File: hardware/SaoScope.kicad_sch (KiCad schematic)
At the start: 24 parts, among them J1 Conn_01x03_Pin, J2 Conn_01x04_Socket, SW1 TS-1077S-AR02016, SW2 TS-1077S-AR02016, SW3 TS-1077S-AR02016, SW4 TS-1077S-AR02016, SW5 TS-1077S-AR02016, U1 STM32G030F6Px, U2 LMC7660, U3 OPA197xDBV, U4 AP2120N-3.0TRG1, X1 Simple_Addon_v2

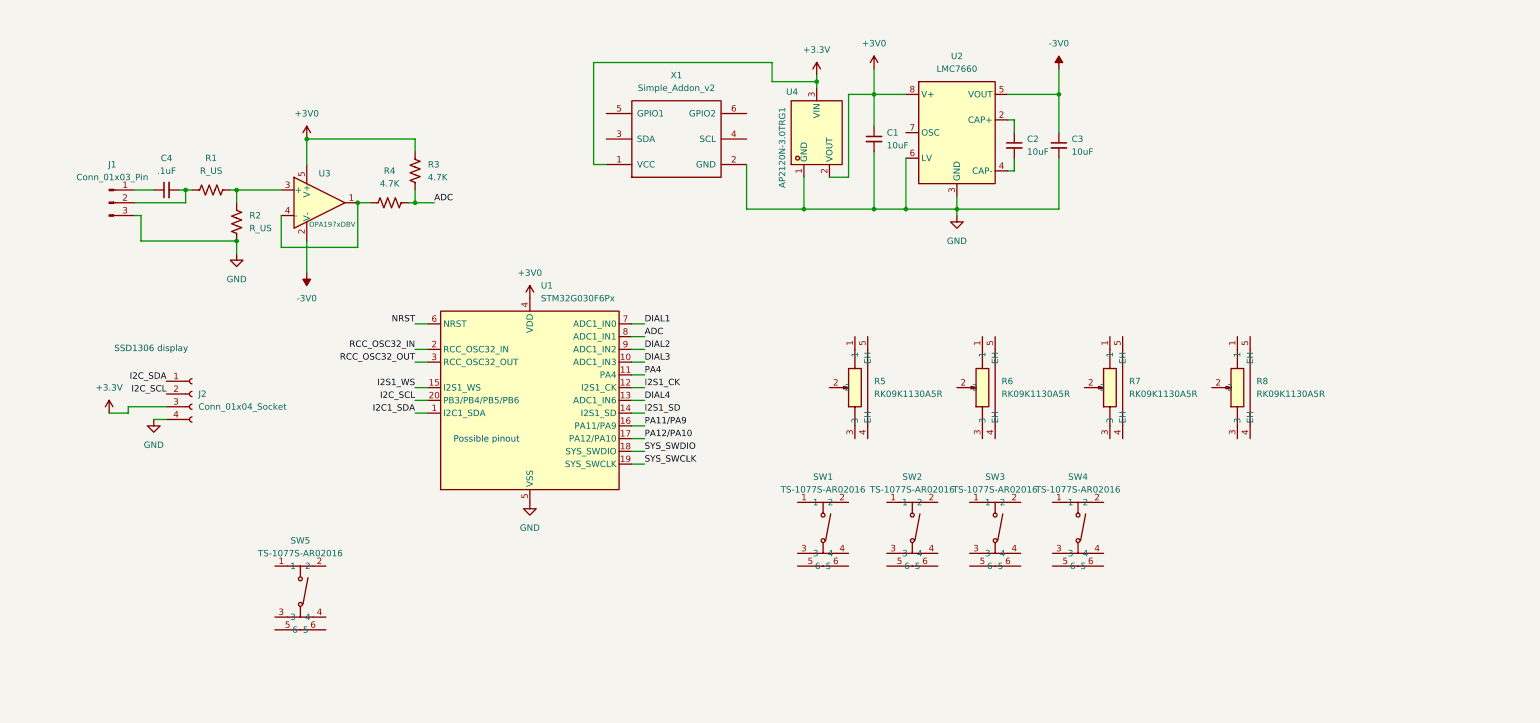
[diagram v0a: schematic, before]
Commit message: wire up pots and buttons, comments
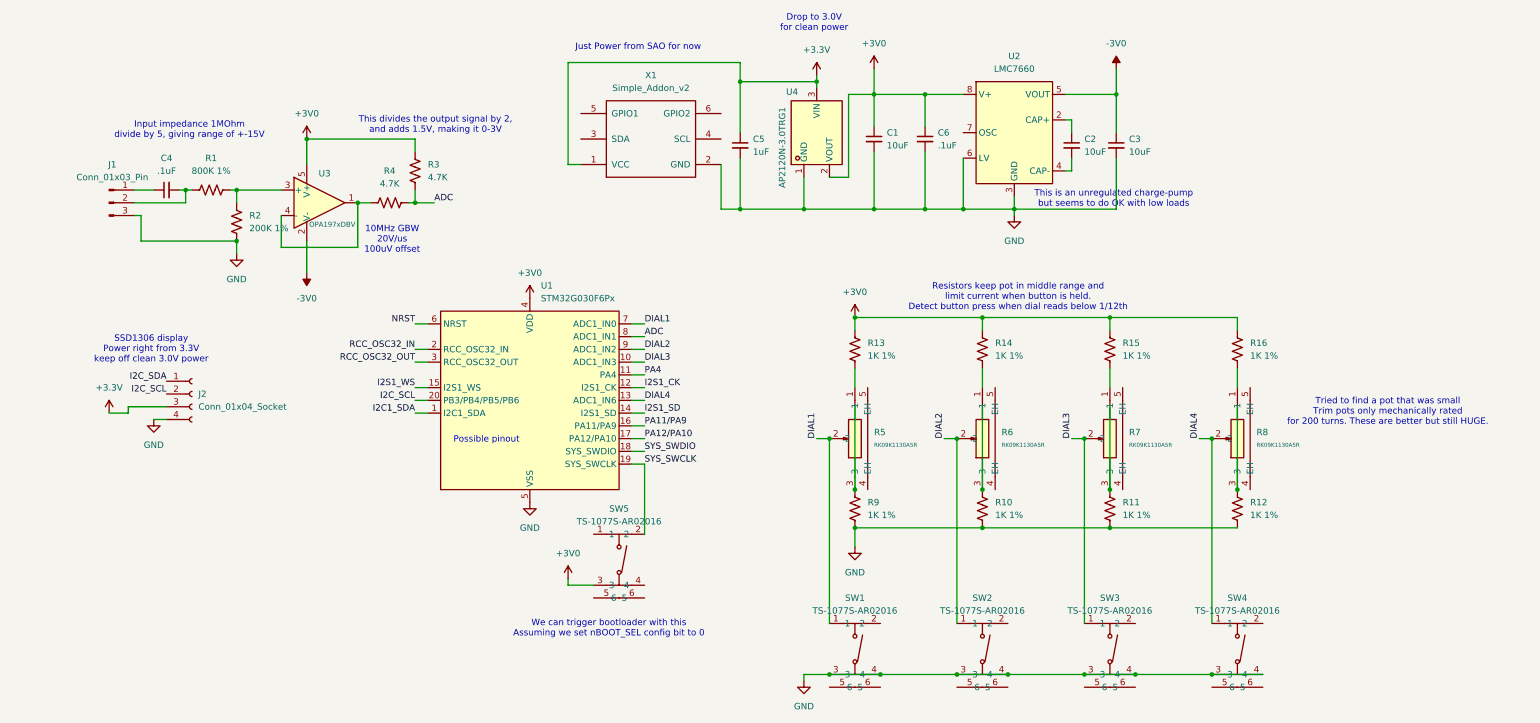
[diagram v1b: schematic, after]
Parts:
- added C5: 1uF, Capacitor_SMD:C_0603_1608Metric, symbol Device:C_Small
- added C6: .1uF, Capacitor_SMD:C_0402_1005Metric, symbol Device:C_Small
- added R10, R11, R12, R13, R14, R15, R16, R9: 1K 1%, Resistor_SMD:R_0402_1005Metric, symbol Device:R_US
- C1, C2, C3: footprint (none) -> Capacitor_SMD:C_0805_2012Metric
- C4: footprint (none) -> Capacitor_SMD:C_0402_1005Metric
- R1: value R_US -> 800K 1%; footprint (none) -> Resistor_SMD:R_0402_1005Metric
- R2: value R_US -> 200K 1%; footprint (none) -> Resistor_SMD:R_0402_1005Metric
- R3, R4: footprint (none) -> Resistor_SMD:R_0402_1005Metric
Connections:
- net +3.3V: now also C5.1
- net +3V0: now also SW5.3, C6.1, R13.1, R14.1, R15.1, R16.1
- net DIAL1: now also R5.2, SW1.1
- net DIAL2: now also R6.2, SW2.1
- net DIAL3: now also R7.2, SW3.1
- net DIAL4: now also R8.2, SW4.1
- net GND: now also SW1.3, SW1.4, SW2.3, SW2.4, SW3.3, SW3.4, SW4.3, SW4.4, C5.2, C6.2, R10.2, R11.2, R12.2, R9.2
- net SYS_SWCLK: now also SW5.2
- net at R5.1: now also R13.2
- net at R5.3: now also R9.1
- net at R6.1: now also R14.2
- net at R6.3: now also R10.1
- net at R7.1: now also R15.2
- net at R7.3: now also R11.1
- net at R8.1: now also R16.2
- net at R8.3: now also R12.1
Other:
- note added: "10MHz GBW 20V/us 100uV offset"
- note added: "Drop to 3.0V for clean power"
- note added: "Input impedance 1MOhm divide by 5, giving range of +-15V"
- note added: "Just Power from SAO for now"
- note added: "Resistors keep pot in middle range and limit current when button is held. Detect button press when dial reads below 1/12th"
- note added: "SSD1306 display Power right from 3.3V keep off clean 3.0V power"
- note added: "This divides the output signal by 2, and adds 1.5V, making it 0-3V"
- note added: "This is an unregulated charge-pump but seems to do OK with low loads"
- note added: "Tried to find a pot that was small Trim pots only mechanically rated for 200 turns. These are better but still HUGE."
- note added: "We can trigger bootloader with this Assuming we set nBOOT_SEL config bit to 0"
- note removed: "SSD1306 display"
- moved on the sheet: C2, C3, R5, R6, R7, R8, SW1, SW2, SW3, SW4, SW5, U2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

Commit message: basic rev
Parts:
- removed R10, R11, R12, R13, R14, R15, R16, R9: 1K 1%, Resistor_SMD:R_0402_1005Metric, symbol Device:R_US
- added C7: .1uF, Capacitor_SMD:C_0402_1005Metric, symbol Device:C_Small
- added C8, C9: 15pf, Capacitor_SMD:C_0402_1005Metric, symbol Device:C_Small
- added RN1, RN2: 1K, Resistor_SMD:R_Array_Convex_4x0402, symbol Device:R_Pack04_Split
- added TP1, TP2, TP3, TP4, TP5: TestPoint, TestPoint:TestPoint_Pad_1.5x1.5mm, symbol Connector:TestPoint
- added Y1: Crystal, Crystal:Crystal_SMD_3215-2Pin_3.2x1.5mm, symbol Device:Crystal
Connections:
- net I2C_SDA is gone; now on net I2C1_SDA: J2.1 (Pin_1)
- net +3.3V: now also TP1.1
- net +3V0: now also SW5.4, C7.1, RN1.6 (R3.2), RN1.8 (R1.2), RN2.6 (R3.2), RN2.8 (R1.2)
- net -3V0: now also C7.2
- net DIAL1: now also SW1.2
- net DIAL2: now also SW2.2
- net DIAL3: now also SW3.2
- net DIAL4: now also SW4.2
- net GND: now also C8.1, C9.1, RN1.5 (R4.2), RN1.7 (R2.2), RN2.5 (R4.2), RN2.7 (R2.2), TP2.1
- net NRST: now also TP5.1
- net SYS_SWCLK: now also SW5.1, TP4.1
- net SYS_SWDIO: now also TP3.1
- net at R6.1: now also RN1.3 (R3.1)
- net at R7.3: now also RN2.2 (R2.1)
- net at J1.2 (Pin_2), R1.1: now also C4.1; no longer C4.2
- net at R8.1: now also RN2.3 (R3.1)
- net at R8.3: now also RN2.4 (R4.1)
- net at J1.1 (Pin_1): now also C4.2; no longer C4.1
- net at R5.3: now also RN1.2 (R2.1)
- net at R7.1: now also RN2.1 (R1.1)
- net at R5.1: now also RN1.1 (R1.1)
- net at R6.3: now also RN1.4 (R4.1)
- net I2C_SCL renamed I2C1_SCL
- net RCC_OSC32_IN: no longer names the net of U1.2 (PC14/PB9)
- net RCC_OSC32_IN: now also C8.2, Y1.1
- net RCC_OSC32_OUT: no longer names the net of U1.3 (PC15)
- net RCC_OSC32_OUT: now also C9.2, Y1.2
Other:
- moved on the sheet: C4

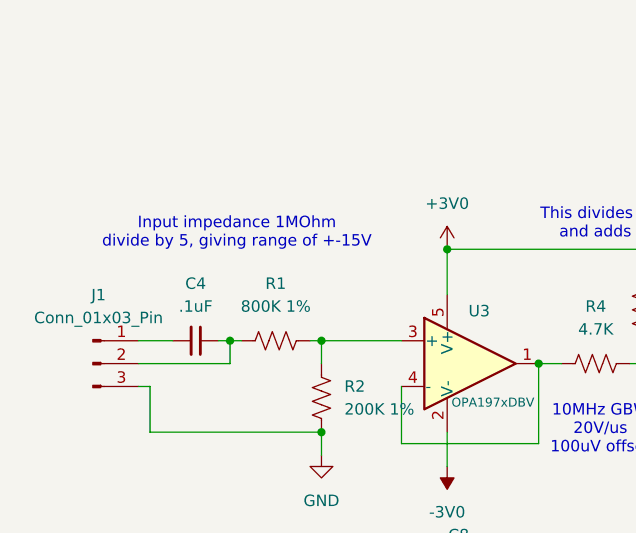
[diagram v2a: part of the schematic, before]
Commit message: switch 800k with two 1.6M resistors
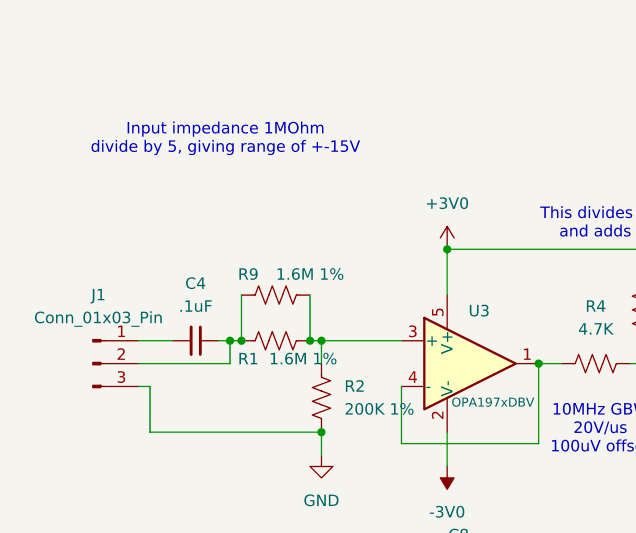
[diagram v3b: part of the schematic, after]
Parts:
- added R9: 1.6M 1%, Resistor_SMD:R_0402_1005Metric, symbol Device:R_US
- R1: value 800K 1% -> 1.6M 1%; LCSC Part (none) -> C172161
- R2: LCSC Part (none) -> C25764
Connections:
- net at C4.1, J1.2 (Pin_2), R1.1: now also R9.1
- net at R1.2, R2.1, U3.3 (+): now also R9.2
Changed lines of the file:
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@@
 	)
 	(junction
+		(at 53.34 63.5)
+		(diameter 0)
+		(color 0 0 0 0)
+	)
+	(junction
 		(at 62.23 73.66)
 		(diameter 0)
@@
 	)
 	(junction
+		(at 60.96 63.5)
+		(diameter 0)
+		(color 0 0 0 0)
+	)
+	(junction
 		(at 162.56 41.91)
 		(diameter 0)
@@
 	(wire
 		(pts
+			(xy 60.96 58.42) (xy 60.96 63.5)
+		)
+		(stroke
+			(width 0)
+			(type default)
+		)
+	)
+	(wire
+		(pts
 			(xy 76.2 73.66) (xy 76.2 77.47)
 		)
@@
 	(wire
 		(pts
+			(xy 53.34 58.42) (xy 53.34 63.5)
+		)
+		(stroke
+			(width 0)
+			(type default)
+		)
+	)
+	(wire
+		(pts
 			(xy 143.51 97.79) (xy 140.97 97.79)
 		)
@@
 	(text "Input impedance 1MOhm\ndivide by 5, giving range of +-15V"
 		(exclude_from_sim no)
-		(at 52.832 51.562 0)
+		(at 51.562 41.148 0)
 		(effects
 			(font
@@
 	)
 	(symbol
+		(lib_id "Device:R_US")
+		(at 57.15 58.42 90)
+		(unit 1)
+		(exclude_from_sim no)
+		(in_bom yes)
+		(on_board yes)
+		(dnp no)
+		(property "Reference" "R9"
+			(at 54.102 56.134 90)
+			(effects
+				(font
+					(size 1.27 1.27)
+				)
+			)
+		)
+		(property "Value" "1.6M 1%"
+			(at 60.96 56.134 90)
+			(effects
+				(font
+					(size 1.27 1.27)
+				)
+			)
+		)
+		(property "Footprint" "Resistor_SMD:R_0402_1005Metric"
+			(at 57.404 57.404 90)
+			(effects
+				(font
+					(size 1.27 1.27)
+				)
+				(hide yes)
+			)
+		)
+		(property "Datasheet" "~"
+			(at 57.15 58.42 0)
+			(effects
+				(font
+					(size 1.27 1.27)
+				)
+				(hide yes)
+			)
+		)
+		(property "Description" "Resistor, US symbol"
+			(at 57.15 58.42 0)
+			(effects
+				(font
+					(size 1.27 1.27)
+				)
+				(hide yes)
+			)
+		)
+		(property "LCSC Part" "C172161"
+			(at 57.15 58.42 90)
+			(effects
+				(font
+					(size 1.27 1.27)
+				)
+				(hide yes)
+			)
+		)
+		(pin "1"
+		)
+		(pin "2"
+		)
+		(instances
+			(project "SaoScope"
+				(path "/a633a3cb-d3b7-422b-9438-b60cd33ff473"
+					(reference "R9")
+					(unit 1)
+				)
+			)
+		)
+	)
+	(symbol
 		(lib_id "Device:R_Pack04_Split")
 		(at 261.62 127 180)
@@
 		(on_board yes)
 		(dnp no)
-		(fields_autoplaced yes)
 		(property "Reference" "R1"
-			(at 57.15 57.15 90)
+			(at 54.102 65.532 90)
 			(effects
 				(font
@@
 			)
 		)
-		(property "Value" "800K 1%"
-			(at 57.15 59.69 90)
+		(property "Value" "1.6M 1%"
+			(at 60.198 65.532 90)
 			(effects
 				(font
@@
 			)
 		)
+		(property "LCSC Part" "C172161"
+			(at 57.15 63.5 90)
+			(effects
+				(font
+					(size 1.27 1.27)
+				)
+				(hide yes)
+			)
+		)
 		(pin "1"
 		)
@@
 			(at 62.23 69.85 0)
 			(effects
+				(font
+					(size 1.27 1.27)
+				)
+				(hide yes)
+			)
+		)
+		(property "LCSC Part" "C25764"
+			(at 62.23 69.85 0)
+			(effects

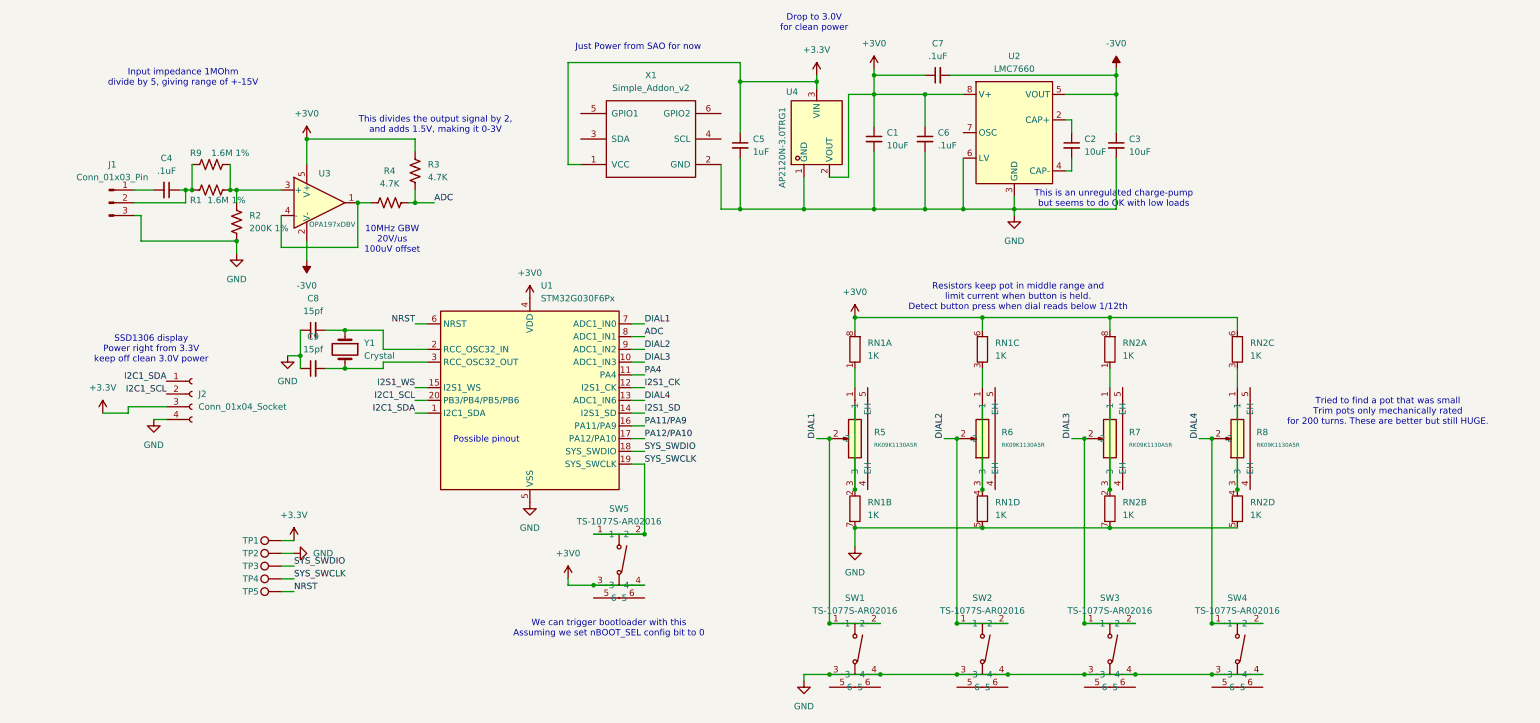
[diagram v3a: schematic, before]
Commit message: bring in i2c lines from sao, a gpio, and run a sig gen line out. rework button labels.
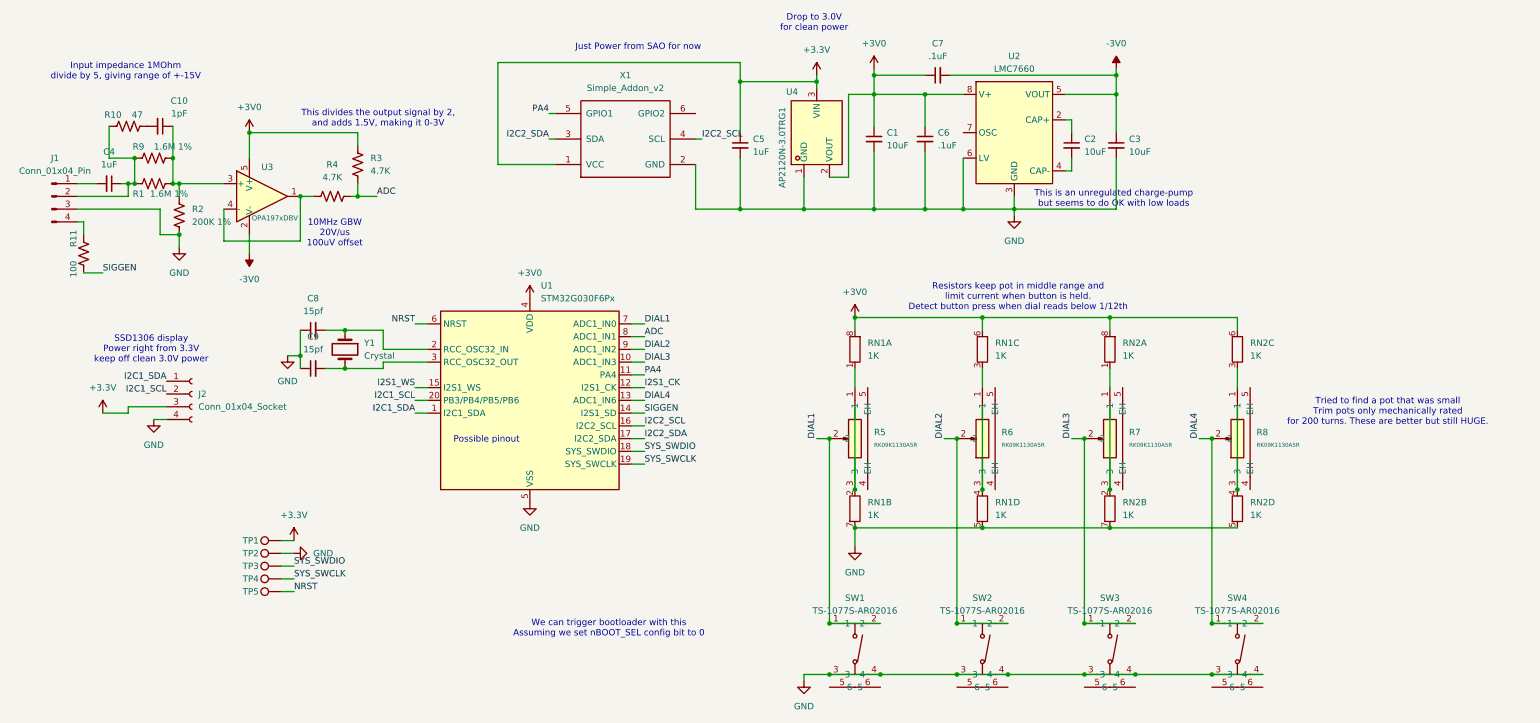
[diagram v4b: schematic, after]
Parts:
- removed J1: Conn_01x03_Pin, Connector_PinHeader_2.54mm:PinHeader_1x03_P2.54mm_Vertical, symbol Connector:Conn_01x03_Pin
- removed SW5: TS-1077S-AR02016, easyeda2kicad:KEY-SMD_4P-L3.1-W3.1-P2.00-LS4.0, symbol easyeda2kicad:TS-1077S-AR02016
- added C10: 1pF, Capacitor_SMD:C_0402_1005Metric, symbol Device:C_Small
- added J1: Conn_01x04_Pin, Connector_PinHeader_2.54mm:PinHeader_1x04_P2.54mm_Vertical, symbol Connector:Conn_01x04_Pin
- added R10: 47, Resistor_SMD:R_0402_1005Metric, symbol Device:R_US
- added R11: 100, Resistor_SMD:R_0402_1005Metric, symbol Device:R_US
- C4: value .1uF -> 1uF; footprint Capacitor_SMD:C_0402_1005Metric -> Capacitor_SMD:C_0603_1608Metric
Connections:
- net PA11/PA9 is gone; now on net I2C2_SCL: U1.16 (PA11/PA9)
- net PA12/PA10 is gone; now on net I2C2_SDA: U1.17 (PA12/PA10)
- net GND: now also J1.3 (Pin_3)
- net PA4: now also X1.5 (GPIO1)
- net at C4.1, R1.1, R9.1: now also J1.2 (Pin_2), R10.1
- net at R1.2, R2.1, R9.2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: now also C10.1
- net at C4.2: now also J1.1 (Pin_1)
- net I2C2_SDA: now reaches X1.3 (SDA)
- net I2C2_SCL: now reaches X1.4 (SCL)
- net I2S1_SD renamed SIGGEN
- net SIGGEN: now also R11.2
- new net: C10.2, R10.2
- new net: J1.4 (Pin_4), R11.1
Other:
- moved on the sheet: C4, R1, R2, R3, R4, R9, U3, X1

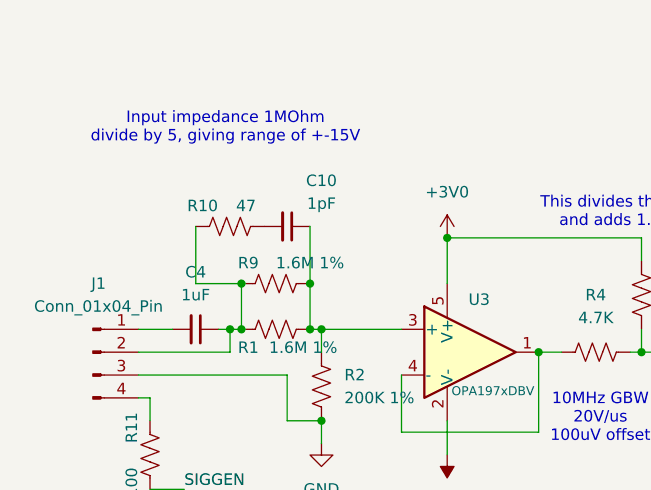
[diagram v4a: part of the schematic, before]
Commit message: fix part number oops
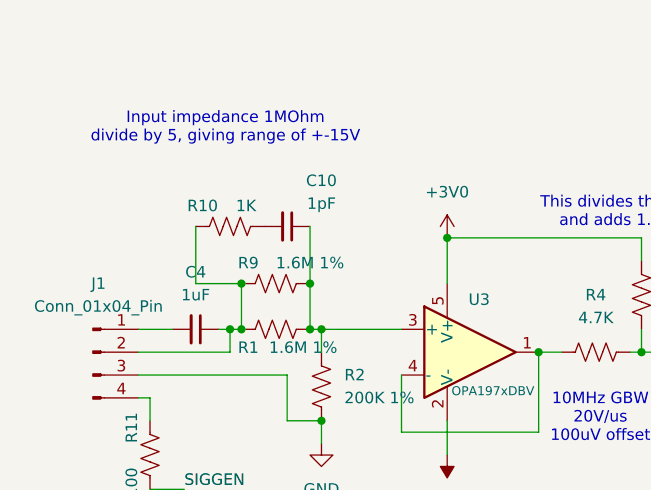
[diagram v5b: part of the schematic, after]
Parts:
- R10: value 47 -> 1K; LCSC Part C172161 -> (none)
- R11: LCSC Part C172161 -> (none)
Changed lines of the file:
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@@
 			)
 		)
-		(property "Value" "47"
+		(property "Value" "1K"
 			(at 42.418 48.514 90)
 			(effects
@@
 			)
 		)
-		(property "LCSC Part" "C172161"
+		(property "LCSC Part" ""
 			(at 40.64 50.8 90)
 			(effects
@@
 			)
 		)
-		(property "LCSC Part" "C172161"
+		(property "LCSC Part" ""
 			(at 31.75 76.2 90)
 			(effects
